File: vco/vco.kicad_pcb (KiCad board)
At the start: 2 copper layers, 61 x 80 mm, 71 parts, among them J1 EXP_FM, J10 SAW, J11 Conn_02x05_Odd_Even, J2 LIN_FM, J3 PWM_IN, J4 CV 1V/OCT, J5 SYNC_IN, J6 SINE, J7 TRI, J8 SQUARE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

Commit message: 8Step sequencer finished with pic
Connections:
- J1 pad G: GND -> Net-(J1-PadG)
- J10 pad G: GND -> Net-(J10-PadG)
- J2 pad G: GND -> Net-(J2-PadG)
- J3 pad G: GND -> Net-(J3-PadG)
- J4 pad G: GND -> Net-(J4-PadG)
- J5 pad G: GND -> Net-(J5-PadG)
- J6 pad G: GND -> Net-(J6-PadG)
- J7 pad G: GND -> Net-(J7-PadG)
- J8 pad G: GND -> Net-(J8-PadG)
- J9 pad G: GND -> Net-(J9-PadG)
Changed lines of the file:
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@@
     (zones 0)
     (modules 71)
-    (nets 65)
+    (nets 75)
   )
   (page A4)
@@
   (net 63 VHFT)
   (net 64 "Net-(RV7-Pad3)")
+  (net 65 "Net-(J1-PadG)")
+  (net 66 "Net-(J2-PadG)")
+  (net 67 "Net-(J3-PadG)")
+  (net 68 "Net-(J4-PadG)")
+  (net 69 "Net-(J5-PadG)")
+  (net 70 "Net-(J6-PadG)")
+  (net 71 "Net-(J7-PadG)")
+  (net 72 "Net-(J8-PadG)")
+  (net 73 "Net-(J9-PadG)")
+  (net 74 "Net-(J10-PadG)")
   (net_class Default "This is the default net class."
     (clearance 0.2)
@@
     (add_net "Net-(C7-Pad2)")
     (add_net "Net-(C8-Pad2)")
+    (add_net "Net-(J1-PadG)")
     (add_net "Net-(J1-PadR)")
     (add_net "Net-(J1-PadT)")
+    (add_net "Net-(J10-PadG)")
     (add_net "Net-(J10-PadR)")
     (add_net "Net-(J10-PadT)")
     (add_net "Net-(J11-Pad4)")
+    (add_net "Net-(J2-PadG)")
     (add_net "Net-(J2-PadR)")
     (add_net "Net-(J2-PadT)")
+    (add_net "Net-(J3-PadG)")
     (add_net "Net-(J3-PadR)")
+    (add_net "Net-(J4-PadG)")
     (add_net "Net-(J4-PadR)")
     (add_net "Net-(J4-PadT)")
+    (add_net "Net-(J5-PadG)")
     (add_net "Net-(J5-PadR)")
+    (add_net "Net-(J6-PadG)")
     (add_net "Net-(J6-PadR)")
     (add_net "Net-(J6-PadT)")
+    (add_net "Net-(J7-PadG)")
     (add_net "Net-(J7-PadR)")
     (add_net "Net-(J7-PadT)")
+    (add_net "Net-(J8-PadG)")
     (add_net "Net-(J8-PadR)")
     (add_net "Net-(J8-PadT)")
+    (add_net "Net-(J9-PadG)")
     (add_net "Net-(J9-PadR)")
     (add_net "Net-(J9-PadT)")
@@
       (net 18 "Net-(J1-PadR)"))
     (pad G thru_hole rect (at -2.54 1.524 180) (size 2.5 1.5) (drill oval 2 1) (layers *.Cu *.Mask)
-      (net 1 GND))
+      (net 65 "Net-(J1-PadG)"))
     (pad S thru_hole rect (at 0 -2.54 180) (size 2.5 1.5) (drill oval 2 1) (layers *.Cu *.Mask)
       (net 1 GND))
@@
       (net 1 GND))
     (pad G thru_hole rect (at -2.54 1.524 180) (size 2.5 1.5) (drill oval 2 1) (layers *.Cu *.Mask)
-      (net 1 GND))
+      (net 66 "Net-(J2-PadG)"))
     (pad R thru_hole rect (at 2.54 0 180) (size 2.5 1.5) (drill oval 2 1) (layers *.Cu *.Mask)
       (net 19 "Net-(J2-PadR)"))
@@
       (net 22 "Net-(J3-PadR)"))
     (pad G thru_hole rect (at -2.54 1.524 180) (size 2.5 1.5) (drill oval 2 1) (layers *.Cu *.Mask)
-      (net 1 GND))
+      (net 67 "Net-(J3-PadG)"))
     (pad S thru_hole rect (at 0 -2.54 180) (size 2.5 1.5) (drill oval 2 1) (layers *.Cu *.Mask)
       (net 1 GND))
@@
       (net 24 "Net-(J4-PadR)"))
     (pad G thru_hole rect (at -2.54 1.524 180) (size 2.5 1.5) (drill oval 2 1) (layers *.Cu *.Mask)
-      (net 1 GND))
+      (net 68 "Net-(J4-PadG)"))
     (pad S thru_hole rect (at 0 -2.54 180) (size 2.5 1.5) (drill oval 2 1) (layers *.Cu *.Mask)
       (net 1 GND))
@@
       (net 1 GND))
     (pad G thru_hole rect (at -2.54 1.524 180) (size 2.5 1.5) (drill oval 2 1) (layers *.Cu *.Mask)
-      (net 1 GND))
+      (net 69 "Net-(J5-PadG)"))
     (pad R thru_hole rect (at 2.54 0 180) (size 2.5 1.5) (drill oval 2 1) (layers *.Cu *.Mask)
       (net 25 "Net-(J5-PadR)"))
@@
       (net 1 GND))
     (pad G thru_hole rect (at -2.54 1.524 180) (size 2.5 1.5) (drill oval 2 1) (layers *.Cu *.Mask)
-      (net 1 GND))
+      (net 70 "Net-(J6-PadG)"))
     (pad R thru_hole rect (at 2.54 0 180) (size 2.5 1.5) (drill oval 2 1) (layers *.Cu *.Mask)
       (net 26 "Net-(J6-PadR)"))
@@
       (net 29 "Net-(J7-PadR)"))
     (pad G thru_hole rect (at -2.54 1.524 180) (size 2.5 1.5) (drill oval 2 1) (layers *.Cu *.Mask)
-      (net 1 GND))
+      (net 71 "Net-(J7-PadG)"))
     (pad S thru_hole rect (at 0 -2.54 180) (size 2.5 1.5) (drill oval 2 1) (layers *.Cu *.Mask)
       (net 1 GND))
@@
       (net 1 GND))
     (pad G thru_hole rect (at -2.54 1.524 180) (size 2.5 1.5) (drill oval 2 1) (layers *.Cu *.Mask)
-      (net 1 GND))
+      (net 72 "Net-(J8-PadG)"))
     (pad R thru_hole rect (at 2.54 0 180) (size 2.5 1.5) (drill oval 2 1) (layers *.Cu *.Mask)
       (net 30 "Net-(J8-PadR)"))
@@
       (net 33 "Net-(J9-PadR)"))
     (pad G thru_hole rect (at -2.54 1.524 180) (size 2.5 1.5) (drill oval 2 1) (layers *.Cu *.Mask)
-      (net 1 GND))
+      (net 73 "Net-(J9-PadG)"))
     (pad S thru_hole rect (at 0 -2.54 180) (size 2.5 1.5) (drill oval 2 1) (layers *.Cu *.Mask)
       (net 1 GND))
@@
       (net 1 GND))
     (pad G thru_hole rect (at -2.54 1.524 180) (size 2.5 1.5) (drill oval 2 1) (layers *.Cu *.Mask)
-      (net 1 GND))
+      (net 74 "Net-(J10-PadG)"))
     (pad R thru_hole rect (at 2.54 0 180) (size 2.5 1.5) (drill oval 2 1) (layers *.Cu *.Mask)
       (net 34 "Net-(J10-PadR)"))

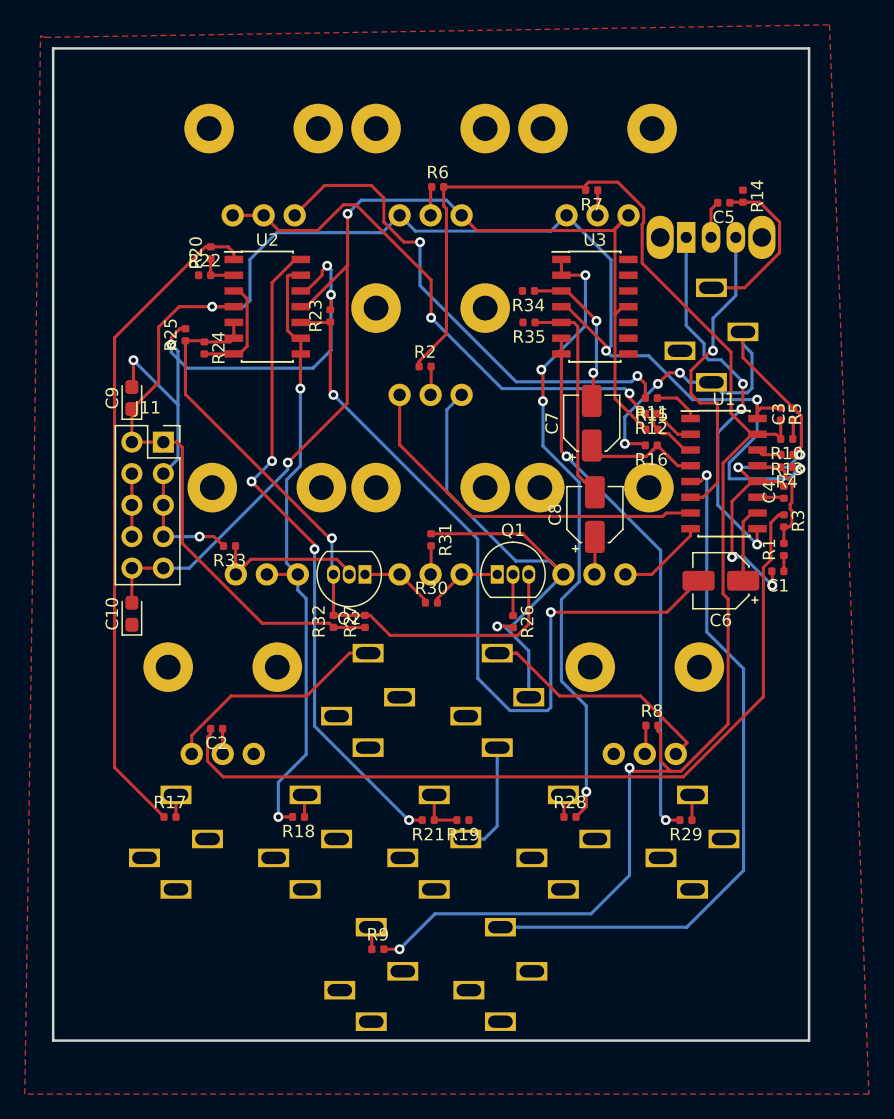
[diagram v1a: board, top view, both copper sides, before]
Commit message: Added vcos infos
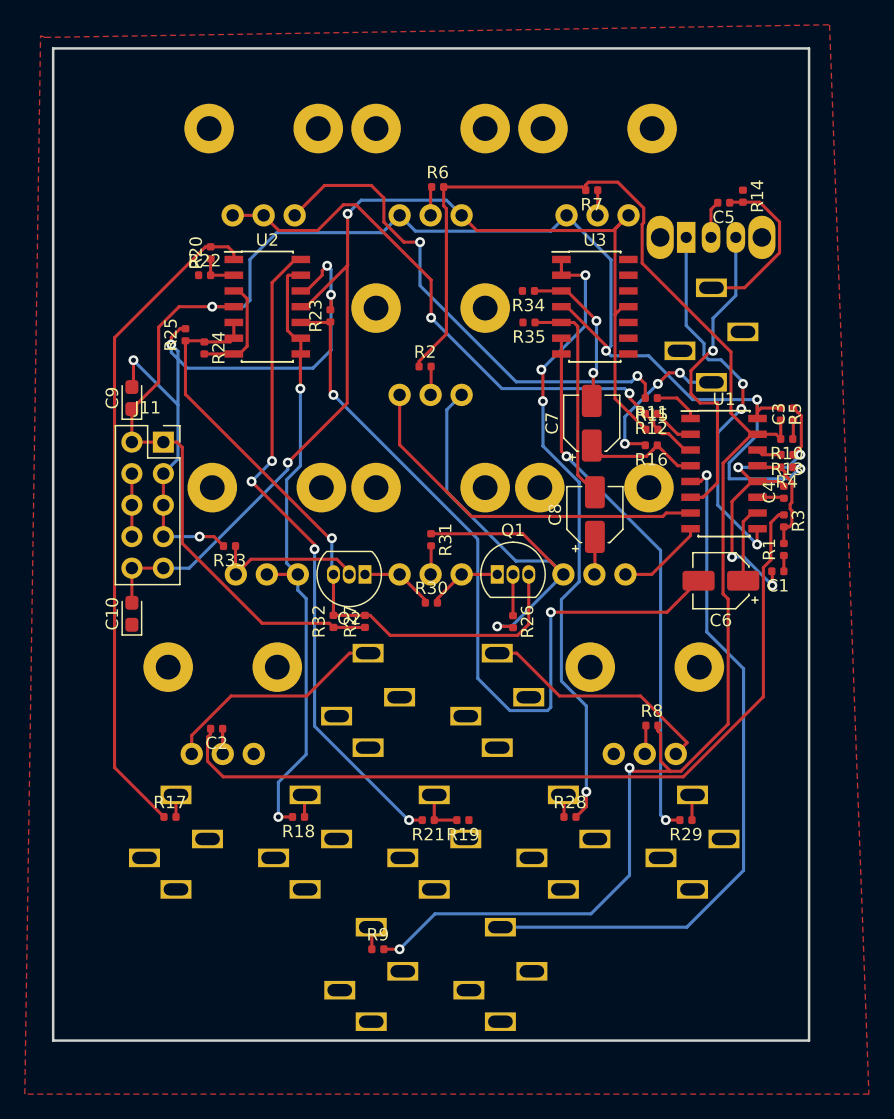
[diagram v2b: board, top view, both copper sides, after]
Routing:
- net GND: track 170.2 -> 138.0 mm
